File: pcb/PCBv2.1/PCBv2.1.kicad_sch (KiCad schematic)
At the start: 17 parts, among them U2 BNO055

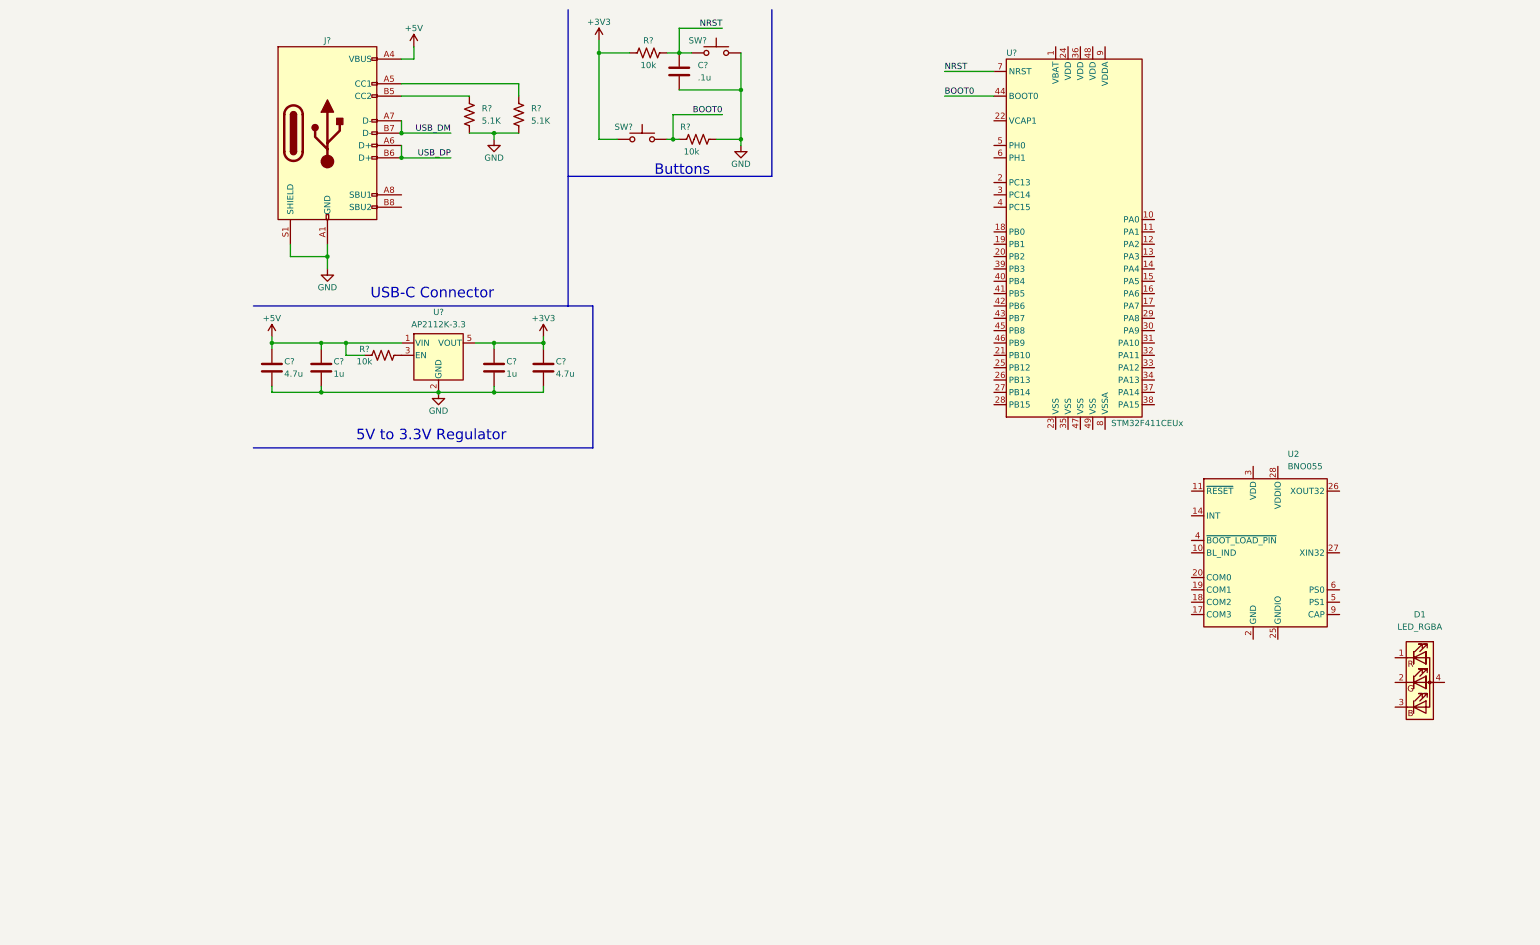
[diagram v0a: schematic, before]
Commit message: Add power supply and leds to pcb
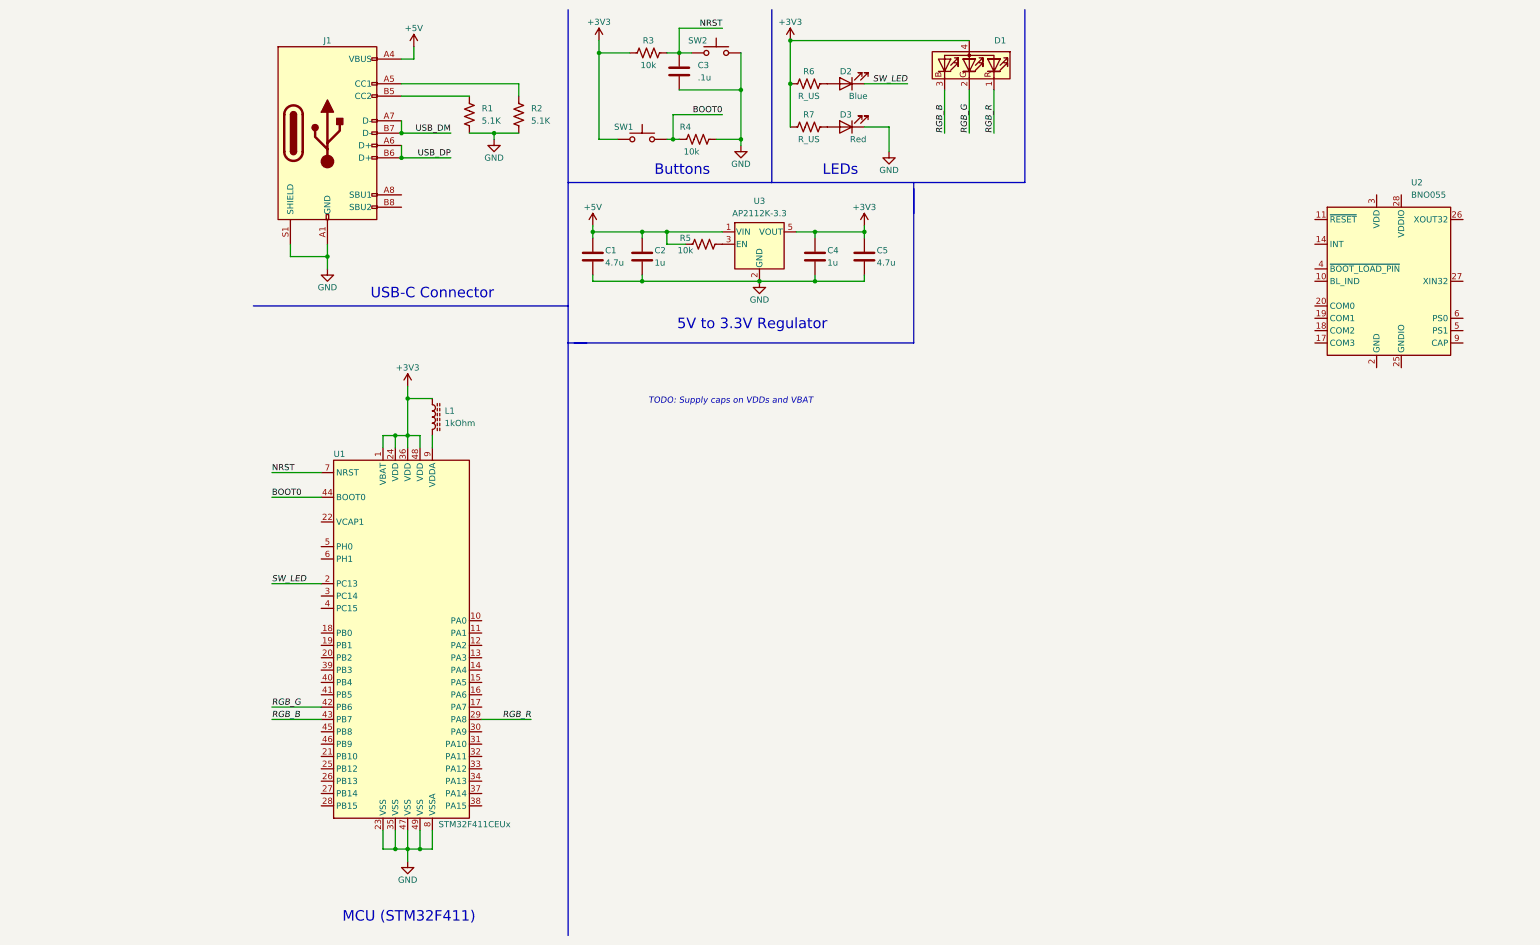
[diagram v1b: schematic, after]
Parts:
- added D2: Blue, symbol Device:LED
- added D3: Red, symbol Device:LED
- added L1: 1kOhm, Inductor_SMD:L_0603_1608Metric_Pad1.05x0.95mm_HandSolder, symbol Device:L_Ferrite
- added R6, R7: R_US, symbol Device:R_US
- gave numbers to parts that had none: 15
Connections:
- net +3V3: now also D1.4 (A), U1.1 (VBAT), U1.24 (VDD), U1.36 (VDD), U1.48 (VDD), L1.1, R6.1, R7.1
- net GND: now also U1.23 (VSS), U1.35 (VSS), U1.47 (VSS), U1.49 (VSS), U1.8 (VSSA), D3.1 (K)
- net SW_LED: now reaches U1.2 (PC13)
- net SW_LED: now also D2.1 (K)
- net RGB_R: now reaches U1.29 (PA8)
- net RGB_R: now also D1.1 (RK)
- net RGB_G: now reaches U1.42 (PB6)
- net RGB_G: now also D1.2 (GK)
- net RGB_B: now reaches U1.43 (PB7)
- net RGB_B: now also D1.3 (BK)
- net at U1.9 (VDDA): now also L1.2
- new net: D2.2 (A), R6.2
- new net: D3.2 (A), R7.2
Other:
- note added: "LEDs"
- note added: "MCU (STM32F411)"
- note added: "TODO: Supply caps on VDDs and VBAT"
- moved on the sheet: C1, C2, C4, C5, D1, R5, U1, U2, U3

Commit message: Labeled all pins in pcb schematic
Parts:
- J1: footprint Connector_USB:USB_C_Receptacle_Palconn_UTC16-G -> (none)
- L1: footprint Inductor_SMD:L_0603_1608Metric_Pad1.05x0.95mm_HandSolder -> Inductor_SMD:L_0805_2012Metric_Pad1.05x1.20mm_HandSolder; Part Number BLM18KN102EH1D -> MFBM1V2012-102-R
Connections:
- net USB_DM: now also U1.32 (PA11)
- net USB_DP: now also U1.33 (PA12)
- net THR8: now reaches U1.10 (PA0)
- net THR7: now reaches U1.11 (PA1)
- net THR6: now reaches U1.12 (PA2)
- net THR5: now reaches U1.13 (PA3)
- net THR4: now reaches U1.16 (PA6)
- net THR3: now reaches U1.17 (PA7)
- net THR2: now reaches U1.18 (PB0)
- net THR1: now reaches U1.19 (PB1)
- net VCAP1: now reaches U1.22 (VCAP1)
- net OSC32_IN: now reaches U1.3 (PC14)
- net SWDIO: now reaches U1.34 (PA13)
- net SWCLK: now reaches U1.37 (PA14)
- net OSC32_OUT: now reaches U1.4 (PC15)
- net SCL1: now reaches U1.45 (PB8)
- net SDA1: now reaches U1.46 (PB9)
- net OSC_IN: now reaches U1.5 (PH0)
- net OSC_OUT: now reaches U1.6 (PH1)
- no-connect marks 0 -> 15
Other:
- note added: "TODO: - Supply caps on VDDs and VBAT - Debug header - Depth sensor header - IMU regulator, level shifter, and interface - VCAP capacitor(s) - Thruster header - oscillators - USB routing (eg line resistors) - Reset line to BNO055? - Other I2C pullup resistors?"
- note removed: "TODO: Supply caps on VDDs and VBAT"
- moved on the sheet: U2

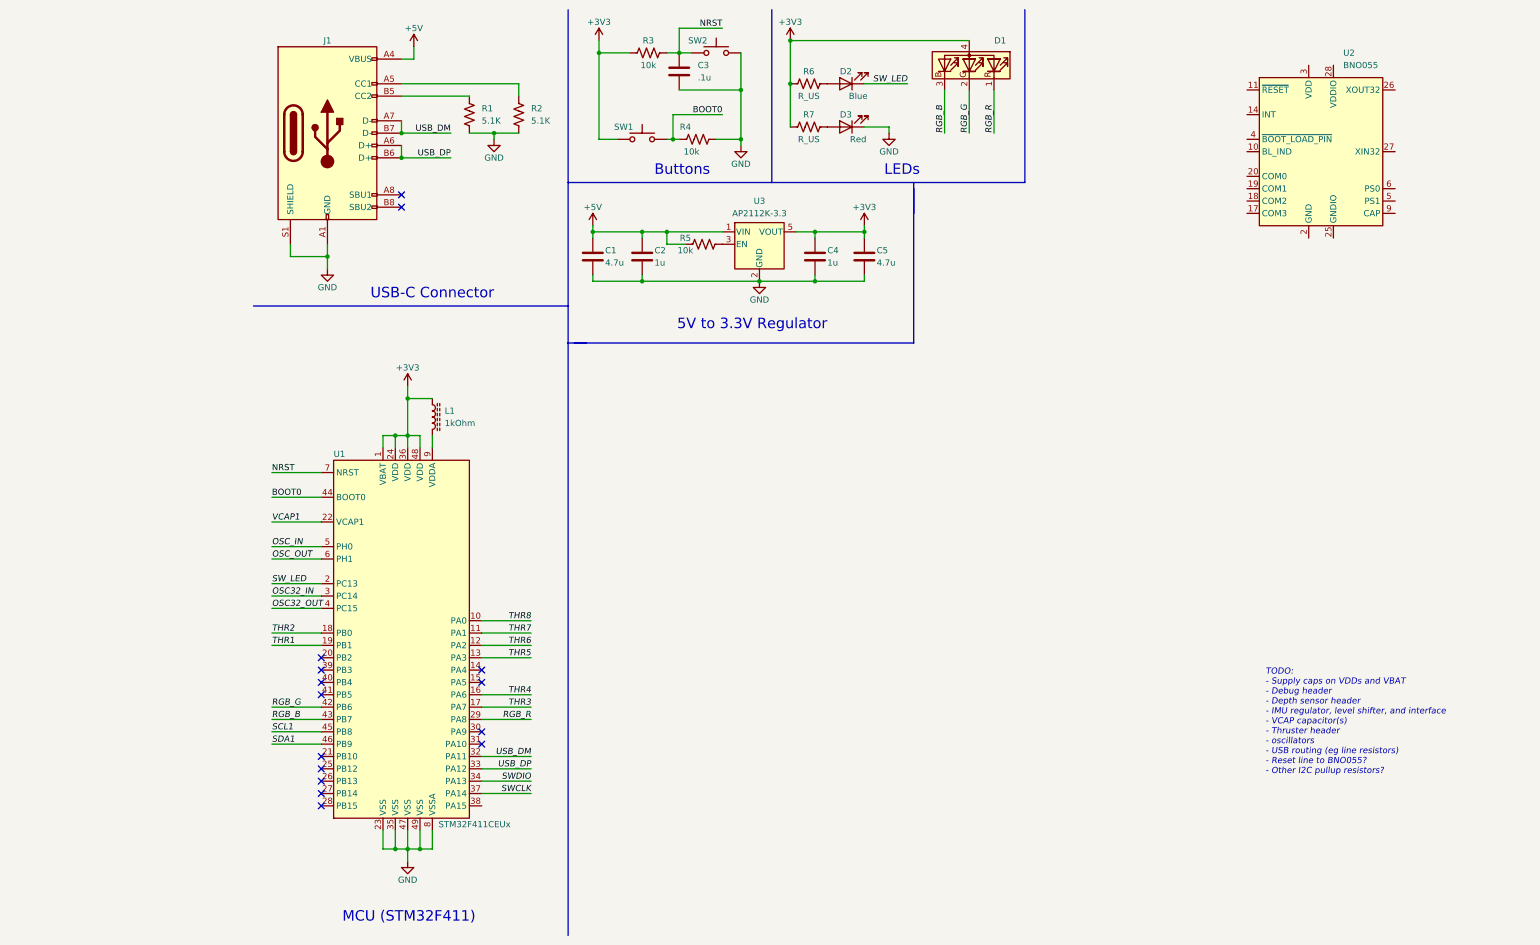
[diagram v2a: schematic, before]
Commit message: Wired IMU in pcb schematic
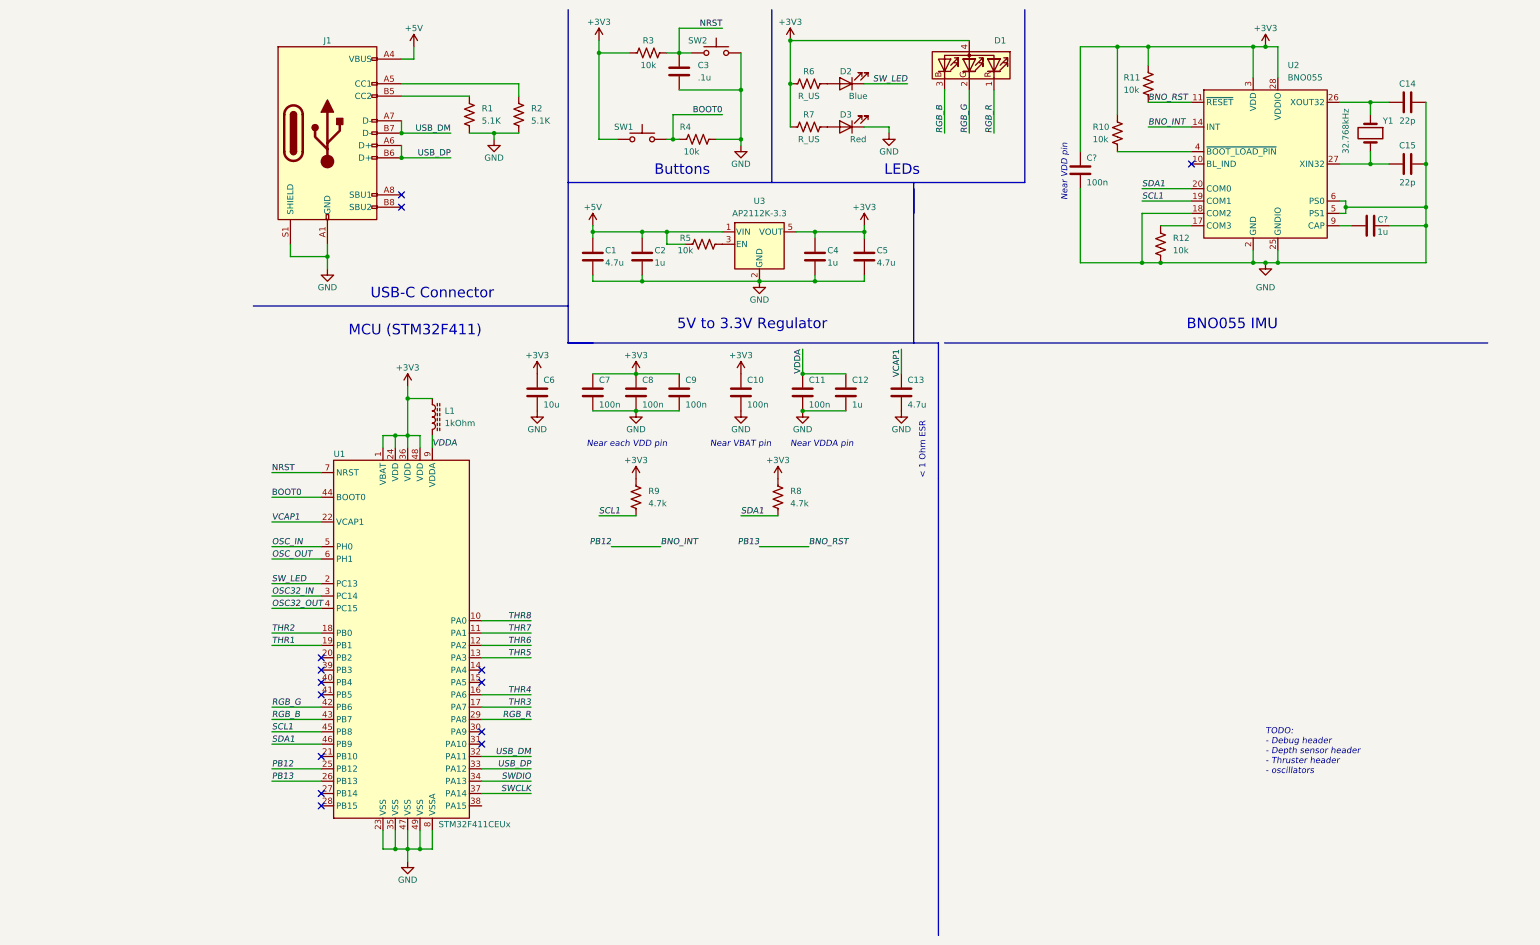
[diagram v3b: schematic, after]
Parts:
- added C10, C11, C7, C8, C9, C?: 100n, symbol Device:C
- added C12, C?: 1u, symbol Device:C
- added C13: 4.7u, symbol Device:C
- added C14, C15: 22p, symbol Device:C
- added C6: 10u, symbol Device:C
- added R10, R11, R12: 10k, symbol Device:R_US
- added R8, R9: 4.7k, symbol Device:R_US
- added Y1: 32.768kHz, symbol Device:Crystal
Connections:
- net +3V3: now also U2.28 (VDDIO), U2.3 (VDD), C10.1, C6.1, C7.1, C8.1, C9.1, C?.1, R10.1, R11.1, R8.1, R9.1
- net GND: now also U2.15 (GNDIO), U2.16 (GNDIO), U2.18 (COM2), U2.2 (GND), U2.25 (GNDIO), U2.5 (PS1), U2.6 (PS0), C10.2, C11.2, C12.2, C13.2, C14.2, C15.2, C6.2, C7.2, C8.2, C9.2, C?.2, C?.2, R12.2
- net SCL1: now also U2.19 (COM1), R9.2
- net SDA1: now also U2.20 (COM0), R8.2
- net VCAP1: now also C13.1
- net BNO_INT: now reaches U1.25 (PB12)
- net BNO_INT: now also U2.14 (INT)
- net BNO_RST: now reaches U1.26 (PB13)
- net BNO_RST: now also U2.11 (~{RESET}), R11.2
- net VDDA: now reaches L1.2, U1.9 (VDDA)
- net VDDA: now also C11.1, C12.1
- net at U2.17 (COM3): now also R12.1
- net at U2.26 (XOUT32): now also C14.1, Y1.1
- net at U2.27 (XIN32): now also C15.1, Y1.2
- net at U2.4 (~{BOOT_LOAD_PIN}): now also R10.2
- net at U2.9 (CAP): now also C?.1
- no-connect marks 15 -> 14
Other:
- note added: "< 1 Ohm ESR"
- note added: "BNO055 IMU"
- note added: "Near VBAT pin"
- note added: "Near VDD pin"
- note added: "Near VDDA pin"
- note added: "Near each VDD pin"
- note added: "TODO: - Debug header - Depth sensor header - Thruster header - oscillators"
- note removed: "TODO: - Supply caps on VDDs and VBAT - Debug header - Depth sensor header - IMU regulator, level shifter, and interface - VCAP capacitor(s) - Thruster header - oscillators - USB routing (eg line resistors) - Reset line to BNO055? - Other I2C pullup resistors?"
- moved on the sheet: U2

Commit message: Add headers to pcb schematic
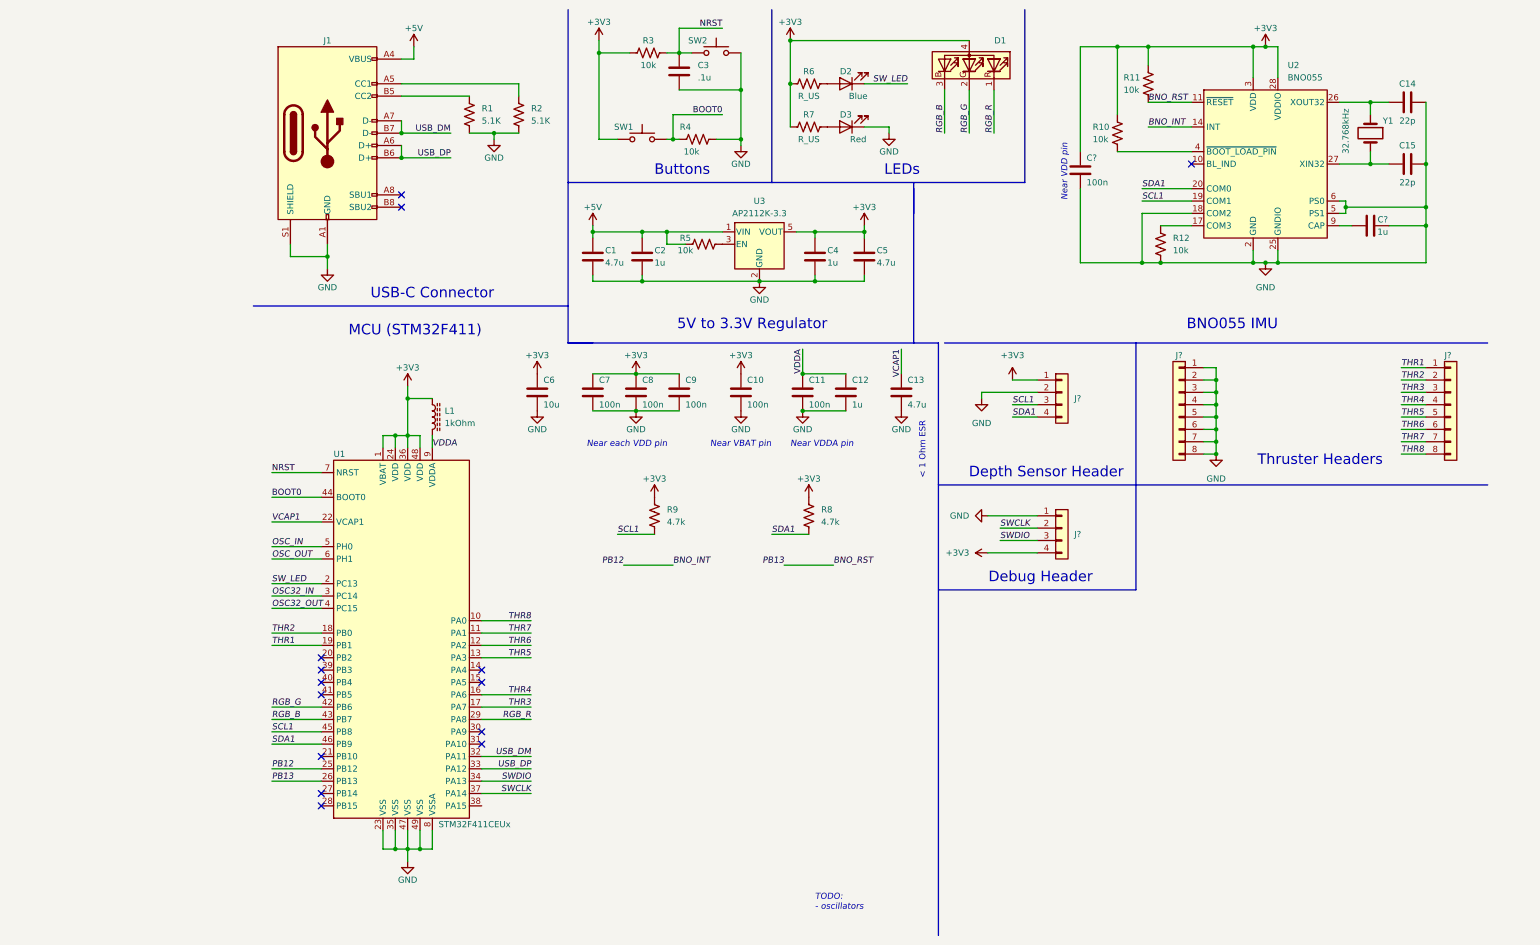
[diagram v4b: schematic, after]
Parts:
- added J? (x2): Conn_01x04, Connector_PinHeader_2.54mm:PinHeader_1x04_P2.54mm_Vertical, symbol Connector_Generic:Conn_01x04
- added J? (x2): Conn_01x08, Connector_PinHeader_2.54mm:PinHeader_1x08_P2.54mm_Vertical, symbol Connector_Generic:Conn_01x08
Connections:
- net +3V3: now also J?.1 (Pin_1), J?.4 (Pin_4)
- net GND: now also J?.1 (Pin_1), J?.1 (Pin_1), J?.2 (Pin_2), J?.2 (Pin_2), J?.3 (Pin_3), J?.4 (Pin_4), J?.5 (Pin_5), J?.6 (Pin_6), J?.7 (Pin_7), J?.8 (Pin_8)
- net SCL1: now also J?.3 (Pin_3)
- net SDA1: now also J?.4 (Pin_4)
- net SWCLK: now also J?.2 (Pin_2)
- net SWDIO: now also J?.3 (Pin_3)
- net THR1: now also J?.1 (Pin_1)
- net THR2: now also J?.2 (Pin_2)
- net THR3: now also J?.3 (Pin_3)
- net THR4: now also J?.4 (Pin_4)
- net THR5: now also J?.5 (Pin_5)
- net THR6: now also J?.6 (Pin_6)
- net THR7: now also J?.7 (Pin_7)
- net THR8: now also J?.8 (Pin_8)
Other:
- note added: "Debug Header"
- note added: "Depth Sensor Header"
- note added: "TODO: - oscillators"
- note added: "Thruster Headers"
- note removed: "TODO: - Debug header - Depth sensor header - Thruster header - oscillators"
- moved on the sheet: R8, R9

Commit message: Finished pcb schematic
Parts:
- added C16, C17: 8p, symbol Device:C
- added C18, C19: 22p, symbol Device:C
- added Y2: 25MHz, symbol Device:Crystal
- added Y3: 32.768kHz, symbol Device:Crystal
- gave numbers to parts that had none: 6
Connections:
- net GND: now also C16.2, C17.2, C18.2, C19.2
- net OSC32_IN: now also C18.1, Y3.1
- net OSC32_OUT: now also C19.1, Y3.2
- net OSC_IN: now also C16.1, Y2.2
- net OSC_OUT: now also C17.1, Y2.1
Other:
- note removed: "TODO: - oscillators"
